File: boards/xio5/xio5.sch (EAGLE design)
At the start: 89 parts, among them IC1 PCAL6416APW,118, J1 98424-G52-14ALF

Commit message: Correct the SPI interface bugs
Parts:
- removed C19: 0.1uF, rcl:C-EUC0201
- removed JP2: (no value), pinhead:PINHD-2X2
- removed JP3: (no value), pinhead-2:PINHD-2X16_2.00
- removed LD_M0, LD_M1: Orange, led:LEDCHIPLED_0603
- removed R1, R6: 59R, rcl:R-EU_R0402
- added C10, C7: 0.1uF, rcl:C-EUC0201
- added IC2: XRA1405IL24-F, samacsys:XRA1405IL24-F
- IC1: value PCAL6416APW,118 -> TC74LCX138FT; device samacsys:PCAL6416APW,118 -> samacsys:TC74LCX138FT
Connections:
- removed net HSPI0_IRQ0: SLOT0.A7, ZTURN-CN2.IO_B35_LN22@CN2_74
- removed net HSPI0_IRQ1: SLOT1.A7, ZTURN-CN2.IO_B35_LP22@CN2_72
- removed net HSPI0_IRQ2: SLOT2.A7, ZTURN-CN2.IO_B35_LN20@CN2_68
- removed net HSPI0_MISO: SLOT0.A4, SLOT1.A4, SLOT2.A4, ZTURN-CN2.IO_B35_LN24@CN2_78
- removed net HSPI0_MOSI: SLOT0.A5, SLOT1.A5, SLOT2.A5, ZTURN-CN2.IO_B35_LP24@CN2_76
- removed net HSPI0_SS0: SLOT0.A6, ZTURN-CN2.IO_B35_LP20@CN2_66
- removed net HSPI0_SS1: SLOT1.A6, ZTURN-CN2.IO_B35_LN18@CN2_64
- removed net HSPI0_SS2: SLOT2.A6, ZTURN-CN2.IO_B35_LP18@CN2_62
- removed net HSPI1_IRQ0: SLOT3.A7, ZTURN-CN2.IO_B35_LN14@CN2_54
- removed net HSPI1_IRQ1: SLOT4.A7, ZTURN-CN2.IO_B35_LP14@CN2_52
- removed net HSPI1_IRQ2: ZTURN-CN2.IO_B35_LN10@CN2_48
- removed net HSPI1_MISO: SLOT3.A4, SLOT4.A4, ZTURN-CN2.IO_B35_LN16@CN2_58
- removed net HSPI1_MOSI: SLOT3.A5, SLOT4.A5, ZTURN-CN2.IO_B35_LP16@CN2_56
- removed net HSPI1_SS0: SLOT3.A6, ZTURN-CN2.IO_B35_LP12@CN2_46
- removed net HSPI1_SS1: SLOT4.A6, ZTURN-CN2.IO_B35_LN10@CN2_44
- removed net HSPI1_SS2: ZTURN-CN2.IO_B35_LP10@CN2_42
- removed net N$2: IC1.P0_7, R6.2
- removed net N$7: IC1.P0_6, R1.2
- removed net N$8: LD_M0.A, R1.1
- removed net SCL: IC1.SCL, JP2.2, ZTURN-I2S-I2C.I2C0_SCL@CN1_78
- removed net SDA: IC1.SDA, JP2.4, ZTURN-I2S-I2C.I2C0_SDA@CN1_76
- removed net SX_PRESENT: IC1.P0_5, JP3.11
- removed net XIO0: IC1.P1_0, JP3.13
- removed net XIO1: IC1.P1_1, JP3.15
- removed net XIO2: IC1.P1_2, JP3.17
- removed net XIO3: IC1.P1_3, JP3.19
- removed net XIO4: IC1.P1_4, JP3.21
- removed net XIO5: IC1.P1_5, JP3.23
- removed net XIO6: IC1.P1_6, JP3.25
- removed net XIO7: IC1.P1_7, JP3.27
- removed net XSPI_IRQ: JP3.5, ZTURN-CN2.IO_B35_LN4@CN2_28
- removed net XSPI_MISO: JP2.1, JP3.7, ZTURN-CN2.IO_B35_LP6@CN2_32
- removed net XSPI_MOSI: JP2.3, JP3.9, ZTURN-CN2.IO_B35_LN6@CN2_34
- new net S5_PRESENT: IC2.P15
- new net SPI1_CLK: SLOT0.A4, SLOT1.A4, SLOT2.A4, SLOT3.A4, SLOT4.A4, ZTURN-CN2.IO_B35_LP22@CN2_72
- new net SPI1_MISO: SLOT0.A5, SLOT1.A5, SLOT2.A5, SLOT3.A5, SLOT4.A5, ZTURN-CN2.IO_B35_LN20@CN2_68
- new net SPI1_MOSI: SLOT0.A6, SLOT1.A6, SLOT2.A6, SLOT3.A6, SLOT4.A6, ZTURN-CN2.IO_B35_LP20@CN2_66
- new net SPI2_CLK: IC2.SCL, ZTURN-CN2.IO_B35_LN16@CN2_58
- new net SPI2_CS0: IC2.CS#, ZTURN-CN2.IO_B35_LN18@CN2_64
- new net SPI2_CS1: ZTURN-CN2.IO_B35_LP18@CN2_62
- new net SPI2_IRQ: IC2.IRQ#, ZTURN-CN2.IO_B35_LP14@CN2_52
- new net SPI2_MISO: IC2.SO, ZTURN-CN2.IO_B35_LP16@CN2_56
- new net SPI2_MOSI: IC2.SI, ZTURN-CN2.IO_B35_LN14@CN2_54
- new net SPI_IRQ0: IC2.P0, SLOT0.A8
- new net SPI_IRQ1: IC2.P1, SLOT1.A8
- new net SPI_IRQ2: IC2.P2, SLOT2.A8
- new net SPI_IRQ3: IC2.P3, SLOT3.A8
- new net SPI_IRQ4: IC2.P4, SLOT4.A8
- new net SPI_IRQ5: IC2.P5
- new net SPI_SS0: IC1.!Y0, SLOT0.A7
- new net SPI_SS1: IC1.!Y1, SLOT1.A7
- new net SPI_SS2: IC1.!Y2, SLOT2.A7
- new net SPI_SS3: IC1.!Y3, SLOT3.A7
- new net SPI_SS4: IC1.!Y4, SLOT4.A7
- new net SPI_SS5: IC1.!Y5
- new net SPI_SS6: IC1.!Y6
- new net SPI_SS7: IC1.!Y7
- net +3V3: now also C10.1, C7.1, IC1.G1, IC1.VCC, IC2.VCC, IC2.VCCP; no longer C19.1, IC1.VDD(I2C-BUS), IC1.VDD(P)
- net +5V: no longer JP3.1, JP3.3
- net GND: now also C10.2, C7.2, IC1.!G2A, IC1.!G2B, IC1.GND, IC2.EP, IC2.GND; no longer C19.2, IC1.ADDR, IC1.VSS, JP3.29, JP3.31, LD_M0.C, LD_M1.C, SLOT0.A8, SLOT1.A8, SLOT2.A8, SLOT3.A8, SLOT4.A8
- net N$3: now also IC1.A, ZTURN-CN2.IO_B35_LN22@CN2_74; no longer LD_M1.A, R6.1
- net N$4: now also IC1.B, ZTURN-CN2.IO_B35_LP24@CN2_76; no longer IC1.!INT, ZTURN-CN2.IO_B35_LP8@CN2_36
- net N$5: now also IC1.C, ZTURN-CN2.IO_B35_LN24@CN2_78; no longer IC1.!RESET, ZTURN-CN2.IO_B35_LN8@CN2_38
- net S0_PRESENT: now also IC2.P10; no longer IC1.P0_0
- net S1_PRESENT: now also IC2.P11; no longer IC1.P0_1
- net S2_PRESENT: now also IC2.P12; no longer IC1.P0_2
- net S3_PRESENT: now also IC2.P13; no longer IC1.P0_3
- net S4_PRESENT: now also IC2.P14; no longer IC1.P0_4
- net ZBUS0: no longer JP3.32
- net ZBUS1: no longer JP3.30
- net ZBUS10: no longer JP3.12
- net ZBUS11: no longer JP3.10
- net ZBUS12: no longer JP3.8
- net ZBUS13: no longer JP3.6
- net ZBUS14: no longer JP3.4
- net ZBUS15: no longer JP3.2
- net ZBUS2: no longer JP3.28
- net ZBUS3: no longer JP3.26
- net ZBUS4: no longer JP3.24
- net ZBUS5: no longer JP3.22
- net ZBUS6: no longer JP3.20
- net ZBUS7: no longer JP3.18
- net ZBUS8: no longer JP3.16
- net ZBUS9: no longer JP3.14
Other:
- note added: "SPI1 runs at ~42 MHz SPI2 runs at ~21 MHz"

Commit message: First pass at a ready-to-go board. Now to debug
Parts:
- added JP2: (no value), pinhead-2:PINHD-2X20_2.00
- added JP3: (no value), pinhead-2:PINHD-2X10_2.00
- added JP4, JP5: (no value), pinhead-2:PINHD-2X04_2.00
- added R1, R6: 22R, rcl:R-EU_R0201
- added U$1: MPBI+, pbxl:MPBI+
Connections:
- new net I2C0_SCL: JP2.37, JP3.4, ZTURN-I2S-I2C.I2C0_SCL@CN1_78
- new net I2C0_SDA: JP2.35, JP3.2, ZTURN-I2S-I2C.I2C0_SDA@CN1_76
- new net N$10: R1.1, ZTURN-CN2.IO_B35_LP22@CN2_72
- new net N$11: R6.1, ZTURN-CN2.IO_B35_LN16@CN2_58
- new net N$2: JP3.10, ZTURN-I2S-I2C.I2S_SCLK@CN1_71
- new net N$6: JP3.12, ZTURN-I2S-I2C.I2S_DIN@CN1_75
- new net N$7: JP3.14, ZTURN-I2S-I2C.I2S_FSYNC_IN@CN1_73
- new net N$8: JP3.16, ZTURN-I2S-I2C.I2S_DOUT@CN1_74
- new net N$9: JP3.18, ZTURN-I2S-I2C.I2S_FSYNC_OUT@CN1_72
- new net S6_PRESENT: IC2.P14, JP4.5
- new net S7_PRESENT: IC2.P15, JP5.5
- new net SPI_IRQ6: IC2.P6, JP4.3
- new net SPI_IRQ7: IC2.P7, JP5.3
- new net XBUS0: JP2.26, JP3.13, ZTURN-CN2.IO_B35_LN4@CN2_28
- new net XBUS1: JP2.28, JP3.15, ZTURN-CN2.IO_B35_LP6@CN2_32
- new net XBUS2: JP2.30, JP3.17, ZTURN-CN2.IO_B35_LN6@CN2_34
- new net XBUS3: JP2.32, JP3.19, ZTURN-CN2.IO_B35_LP8@CN2_36
- new net XBUS4: JP2.34, ZTURN-CN2.IO_B35_LN8@CN2_38
- new net XBUS5: JP2.36, ZTURN-CN2.IO_B35_LP10@CN2_42
- new net XBUS6: JP2.38, ZTURN-CN2.IO_B35_LN10@CN2_44
- new net XBUS7: JP2.40, ZTURN-CN2.IO_B35_LP12@CN2_46
- new net XBUS8: ZTURN-CN2.IO_B35_LN10@CN2_48
- net !HI_CCTL!: now also U$1.!CCTL!@30
- net !HI_EXTSEL!: now also U$1.!EXT!@26
- net !HI_HALT!: now also U$1.!HLT!@33
- net !HI_IRQ!: now also U$1.!IRQ!@23
- net !HI_MPD!: now also U$1.!MPD!@25
- net !HI_RST!: now also U$1.!RST!@31
- net !HI_S4!: now also U$1.!S4!@37
- net !HI_S5!: now also U$1.!S5!@39
- net +3V3: now also JP2.6, JP2.8, JP3.5, JP3.7
- net +5V: now also JP2.2, JP2.4, JP3.1, JP3.3, JP4.1, JP5.1, U$1.+5V@17
- net GND: now also JP2.24, JP2.33, JP2.39, JP3.11, JP3.20, JP3.6, JP3.8, JP3.9, JP4.7, JP4.8, JP5.7, JP5.8, U$1.GND@35
- net HI_A0: now also U$1.A0@16
- net HI_A1: now also U$1.A1@14
- net HI_A10: now also U$1.A10@46
- net HI_A11: now also U$1.A11@44
- net HI_A12: now also U$1.A12@42
- net HI_A13: now also U$1.A13@40
- net HI_A14: now also U$1.A14@38
- net HI_A15: now also U$1.A15@36
- net HI_A2: now also U$1.A2@12
- net HI_A3: now also U$1.A3@10
- net HI_A4: now also U$1.A4@8
- net HI_A5: now also U$1.A5@6
- net HI_A6: now also U$1.A6@4
- net HI_A7: now also U$1.A7@2
- net HI_A8: now also U$1.A8@50
- net HI_A9: now also U$1.A9@48
- net HI_CLK: now also U$1.B02@29
- net HI_D0: now also U$1.D0@15
- net HI_D1: now also U$1.D1@13
- net HI_D2: now also U$1.D2@11
- net HI_D3: now also U$1.D3@9
- net HI_D4: now also U$1.D4@7
- net HI_D5: now also U$1.D5@5
- net HI_D6: now also U$1.D6@3
- net HI_D7: now also U$1.D7@1
- net HI_R/!W!: now also U$1.R/!W!@27
- net HI_RD4: now also U$1.RD4@43
- net HI_RD5: now also U$1.RD5@45
- net S0_PRESENT: now also IC2.P8; no longer IC2.P10
- net S1_PRESENT: now also IC2.P9; no longer IC2.P11
- net S2_PRESENT: now also IC2.P10; no longer IC2.P12
- net S3_PRESENT: now also IC2.P11; no longer IC2.P13
- net S4_PRESENT: now also IC2.P12; no longer IC2.P14
- net S5_PRESENT: now also IC2.P13, JP2.20; no longer IC2.P15
- net SPI1_CLK: now also JP4.2, JP5.2, R1.2; no longer ZTURN-CN2.IO_B35_LP22@CN2_72
- net SPI1_MISO: now also JP4.4, JP5.4
- net SPI1_MOSI: now also JP4.6, JP5.6
- net SPI2_CLK: now also JP2.10, R6.2; no longer ZTURN-CN2.IO_B35_LN16@CN2_58
- net SPI2_CS1: now also JP2.12
- net SPI2_IRQ: now also JP2.16
- net SPI2_MISO: now also JP2.14
- net SPI2_MOSI: now also JP2.18
- net SPI_IRQ5: now also JP2.22
- net ZBUS0: now also JP2.31
- net ZBUS1: now also JP2.29
- net ZBUS10: now also JP2.11
- net ZBUS11: now also JP2.9
- net ZBUS12: now also JP2.7
- net ZBUS13: now also JP2.5
- net ZBUS14: now also JP2.3
- net ZBUS15: now also JP2.1
- net ZBUS2: now also JP2.27
- net ZBUS3: now also JP2.25
- net ZBUS4: now also JP2.23
- net ZBUS5: now also JP2.21
- net ZBUS6: now also JP2.19
- net ZBUS7: now also JP2.17
- net ZBUS8: now also JP2.15
- net ZBUS9: now also JP2.13
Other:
- note added: "Audio interface"
- note added: "SPI1 runs at ~42 MHz SPI2 runs at ~21 MHz For 6 mil trace, 4" has ~59R impedance"
- note added: "Slots 4 & X"
- note removed: "SPI1 runs at ~42 MHz SPI2 runs at ~21 MHz"
- note removed: "Slot 4"
- moved on the sheet: ZTURN-I2S-I2C

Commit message: Start the process of verifying the schematic
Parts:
- U$1: NOSTUFF (none) -> 1
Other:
- note added: "!EXTSEL!, !MPD! and !IRQ! have internal pullups on the Atari Motherboard"
- note added: "+5V Card-present Slot ID"
- note added: "+5V Slot 3.3v Card-present Slot ID"
- note added: "B1,2,3 B4 A1,2,3"
- note added: "B1,2,3 B5,6,7 B4 A1,2,3"
- note added: "Parts Verified"
- note removed: "+5V Card-present Slot ID GND"
- note removed: "+5V Slot 3.3v Card-present Slot ID GND"
- note removed: "/18"
- note removed: "B1,2,3 B4 A1,2,3 A4,5,6,7"
- note removed: "B1,2,3 B5,6,7 B4 A1,2,3 A4,5,6,7"
- moved on the sheet: C1, C10, C11, C12, C13, C14, C15, C16, C17, C18, C2, C3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

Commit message: Board parts verified. Circuit to be checked. BOM manipulated a bit, save $500 @ q50, or $140 @ q5
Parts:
- H3, H6, H7, H8, JP1, JP4, JP5, ZTURN: NOSTUFF (none) -> 1
- IC1: value TC74LCX138FT -> SN74LVC138APWR; USE (none) -> SN74LVC138APWR
- IC2: USE (none) -> XRA1405IL24-F
- J1: USE (none) -> 98424-G52-14ALF
- JP2: USE (none) -> SBH21-NBPN-D20-ST-BK

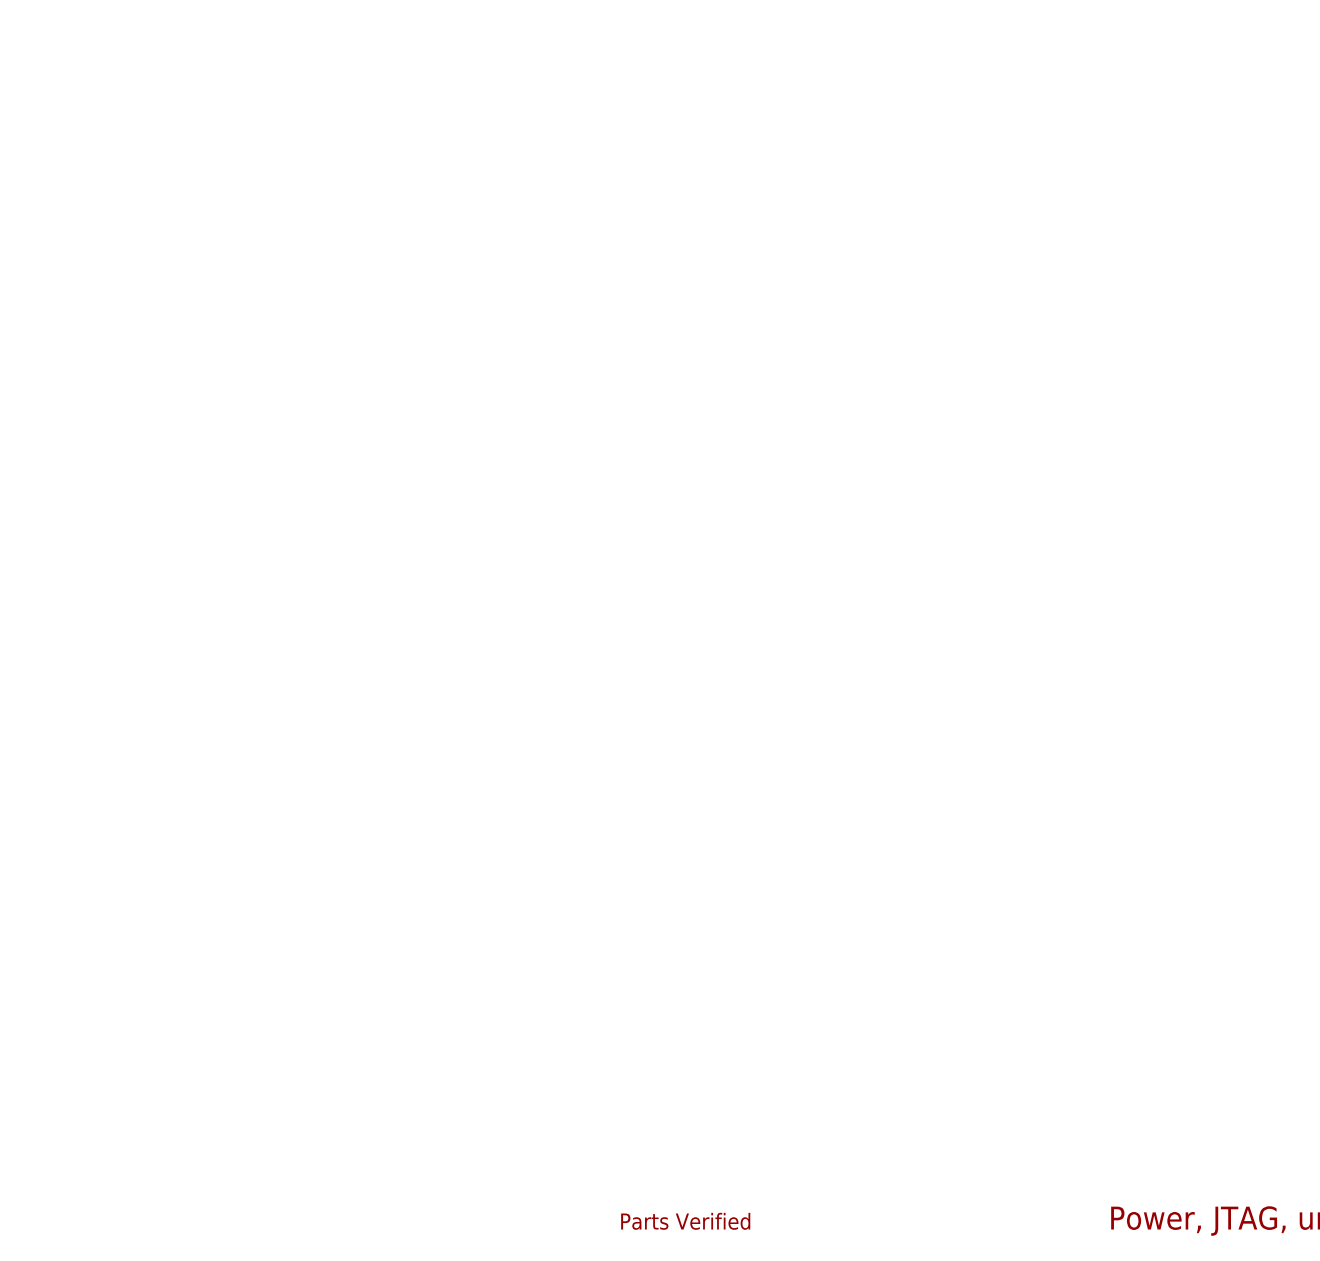
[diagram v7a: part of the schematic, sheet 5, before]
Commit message: Add two connectors to stand in for the Zynq board
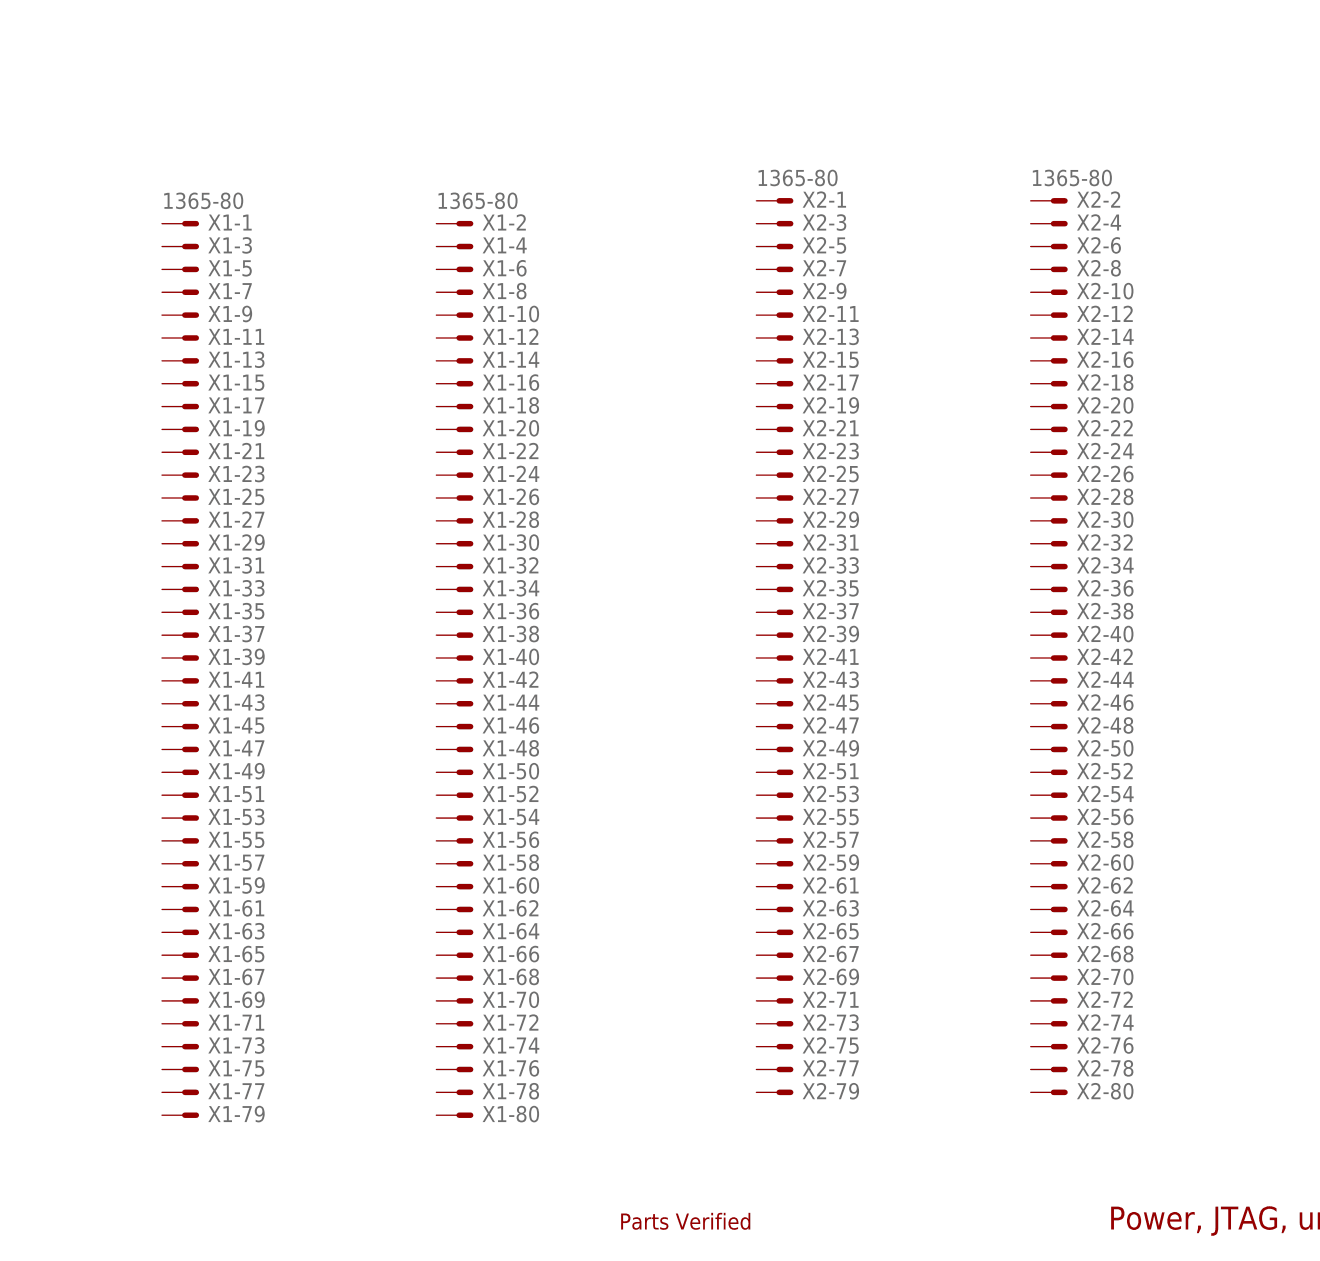
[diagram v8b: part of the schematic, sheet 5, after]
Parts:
- added X1, X2: 1365-80, con-leotronics:1365-80
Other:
- note added: "Ethernet"
- note added: "USB"
